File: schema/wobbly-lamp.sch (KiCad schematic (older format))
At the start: 29 parts, among them IC1 ATMEGA8-AI, Q1 IRLML0030TRPbF, Q2 IRLML0030TRPbF, Q3 IRLML0030TRPbF, U1 LD1117S33TR

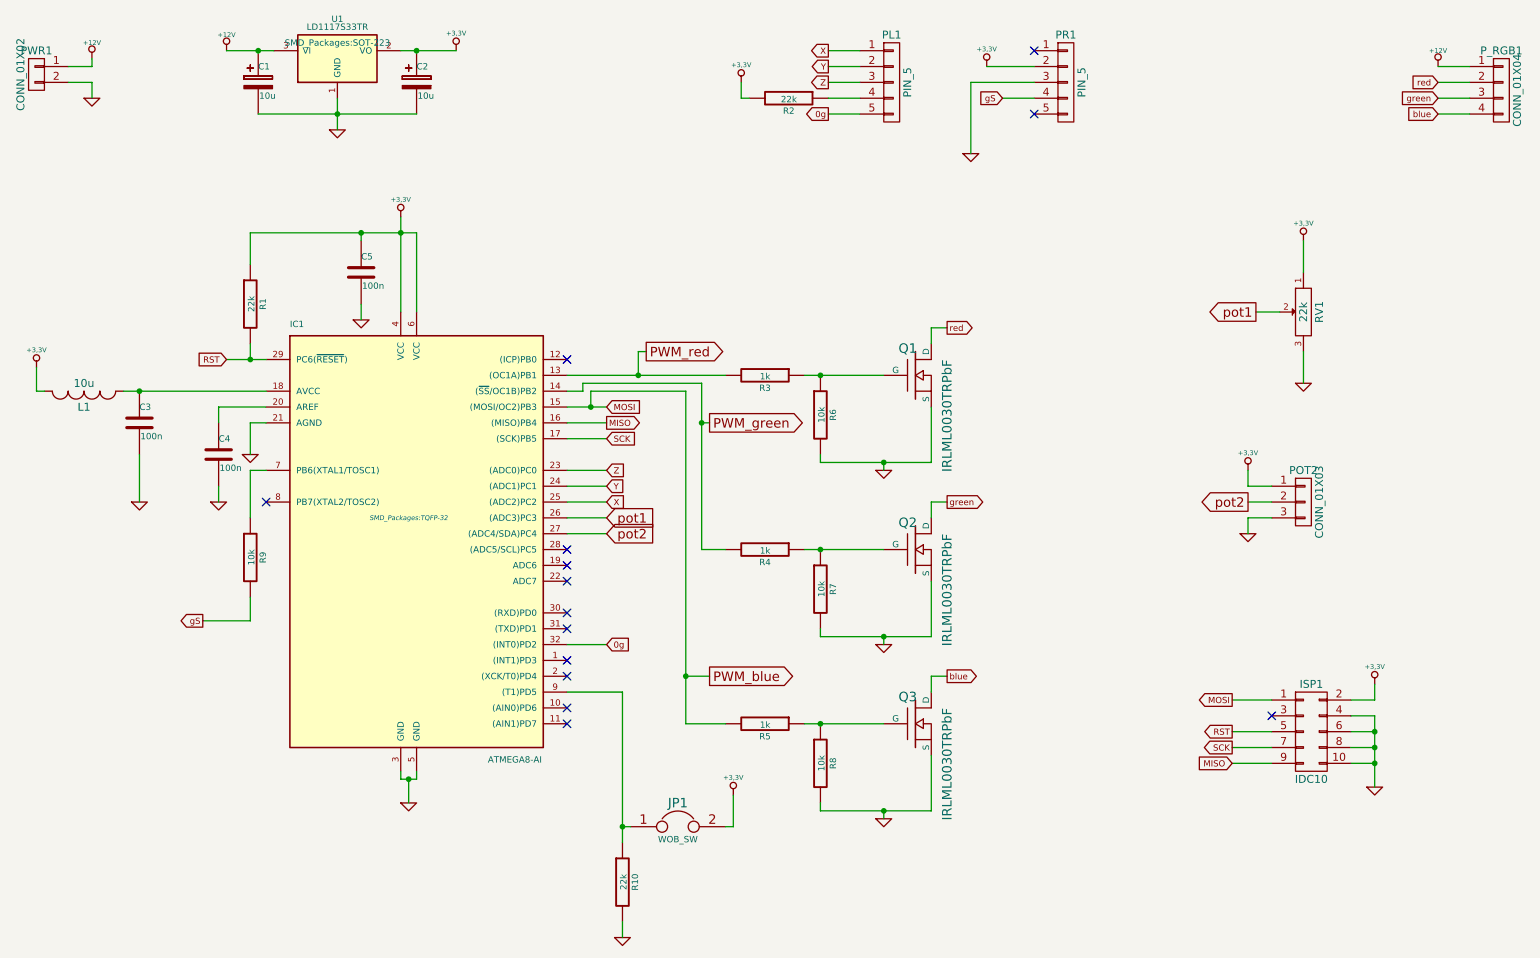
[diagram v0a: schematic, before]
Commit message: Add first working PCB, tiny version
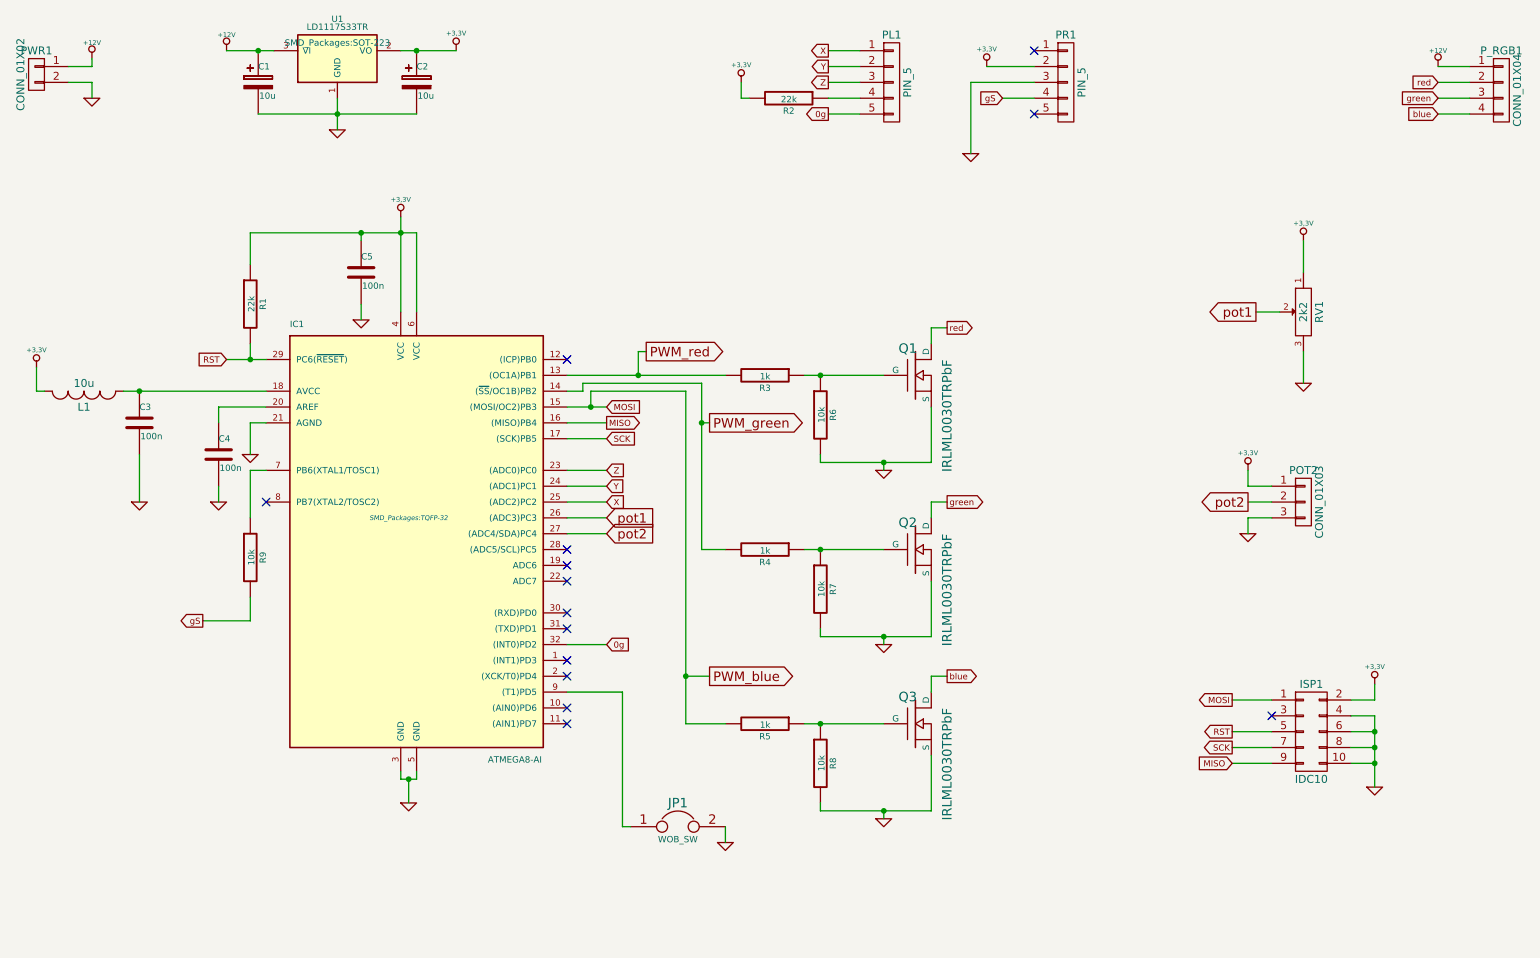
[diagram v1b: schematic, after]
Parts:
- removed R10: 22k, Resistors_SMD:R_0805_HandSoldering, symbol R
- Q1, Q2, Q3: footprint Transistors_SMD:SOT23_FET-D+GS -> Housings_SOT-23_SOT-143_TSOT-6:SOT23_FET_Handsoldering
- RV1: value 22k -> 2k2
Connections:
- net +3.3V: no longer JP1.2
- net GND: now also JP1.2
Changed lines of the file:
@@
 F 0 "Q1" H 6660 3220 60  0000 R CNN
 F 1 "IRLML0030TRPbF" V 6850 3150 60  0000 R CNN
-F 2 "Transistors_SMD:SOT23_FET-D+GS" H 6650 3050 60  0001 C CNN
+F 2 "Housings_SOT-23_SOT-143_TSOT-6:SOT23_FET_Handsoldering" H 6650 3050 60  0001 C CNN
 F 3 "" H 6650 3050 60  0000 C CNN
 	1    6650 3050
@@
 F 0 "Q2" H 6660 4320 60  0000 R CNN
 F 1 "IRLML0030TRPbF" V 6850 4250 60  0000 R CNN
-F 2 "Transistors_SMD:SOT23_FET-D+GS" H 6650 4150 60  0001 C CNN
+F 2 "Housings_SOT-23_SOT-143_TSOT-6:SOT23_FET_Handsoldering" H 6650 4150 60  0001 C CNN
 F 3 "" H 6650 4150 60  0000 C CNN
 	1    6650 4150
@@
 F 0 "Q3" H 6660 5420 60  0000 R CNN
 F 1 "IRLML0030TRPbF" V 6850 5350 60  0000 R CNN
-F 2 "Transistors_SMD:SOT23_FET-D+GS" H 6650 5250 60  0001 C CNN
+F 2 "Housings_SOT-23_SOT-143_TSOT-6:SOT23_FET_Handsoldering" H 6650 5250 60  0001 C CNN
 F 3 "" H 6650 5250 60  0000 C CNN
 	1    6650 5250
@@
 	4850 5900 4800 5900
 Wire Wire Line
-	4800 5050 4800 6000
-Wire Wire Line
 	4800 5050 4450 5050
-$Comp
-L +3,3V #PWR022
-U 1 1 547516A7
-P 5500 5700
-F 0 "#PWR022" H 5500 5660 30  0001 C CNN
-F 1 "+3,3V" H 5500 5810 30  0000 C CNN
-F 2 "" H 5500 5700 60  0000 C CNN
-F 3 "" H 5500 5700 60  0000 C CNN
-	1    5500 5700
-	1    0    0    -1
-$EndComp
-Wire Wire Line
-	5500 5700 5500 5900
-Wire Wire Line
-	5500 5900 5450 5900
-$Comp
-L R R10
-U 1 1 5475179B
-P 4800 6250
-F 0 "R10" V 4880 6250 40  0000 C CNN
-F 1 "22k" V 4807 6251 40  0000 C CNN
-F 2 "Resistors_SMD:R_0805_HandSoldering" V 4730 6250 30  0001 C CNN
-F 3 "" H 4800 6250 30  0000 C CNN
-	1    4800 6250
-	1    0    0    -1
-$EndComp
 $Comp
 L GND #PWR023
 U 1 1 547517D5
-P 4800 6600
-F 0 "#PWR023" H 4800 6600 30  0001 C CNN
-F 1 "GND" H 4800 6530 30  0001 C CNN
-F 2 "" H 4800 6600 60  0000 C CNN
-F 3 "" H 4800 6600 60  0000 C CNN
-	1    4800 6600
-	1    0    0    -1
-$EndComp
-Wire Wire Line
-	4800 6600 4800 6500
-Connection ~ 4800 5900
+P 5450 6000
+F 0 "#PWR023" H 5450 6000 30  0001 C CNN
+F 1 "GND" H 5450 5930 30  0001 C CNN
+F 2 "" H 5450 6000 60  0000 C CNN
+F 3 "" H 5450 6000 60  0000 C CNN
+	1    5450 6000
+	1    0    0    -1
+$EndComp
+Wire Wire Line
+	5450 6000 5450 5900
 Wire Wire Line
 	4450 3950 4700 3950
@@
 P 9100 2650
 F 0 "RV1" H 9100 2550 50  0000 C CNN
-F 1 "22k" H 9100 2650 50  0000 C CNN
+F 1 "2k2" H 9100 2650 50  0000 C CNN
 F 2 "Potentiometers:Potentiometer_VishaySpectrol-Econtrim-Type36T" H 9100 2650 60  0001 C CNN
 F 3 "" H 9100 2650 60  0000 C CNN
@@
 Wire Wire Line
 	9100 2900 9100 3100
+Wire Wire Line
+	4800 5900 4800 5050
 $EndSCHEMATC
